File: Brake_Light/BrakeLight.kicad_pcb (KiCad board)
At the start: 2 copper layers, 99 x 20 mm, 38 parts, among them J2 Conn_01x01_Socket, J3 Conn_01x01_Socket, U1 LM317MABDTG

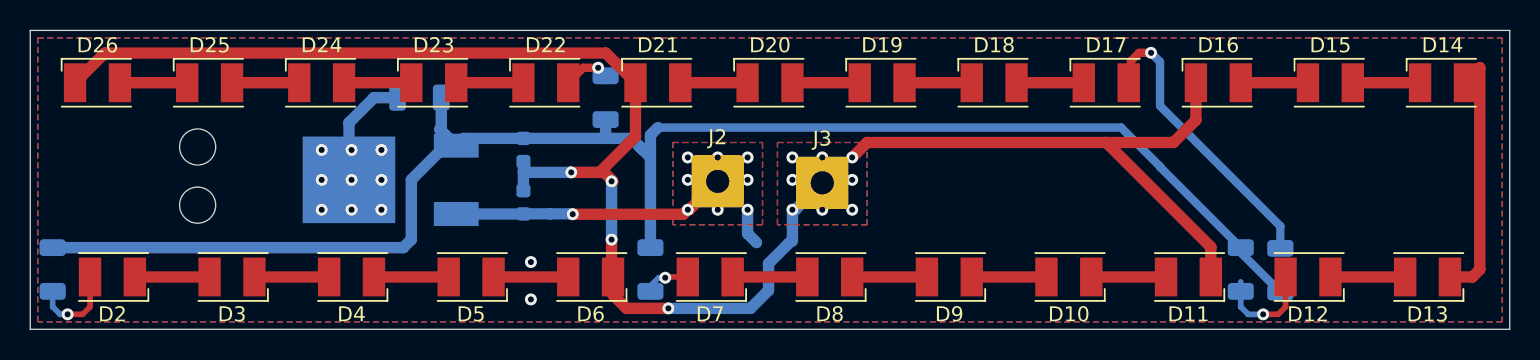
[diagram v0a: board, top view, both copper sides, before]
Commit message: Upgrade zones and via
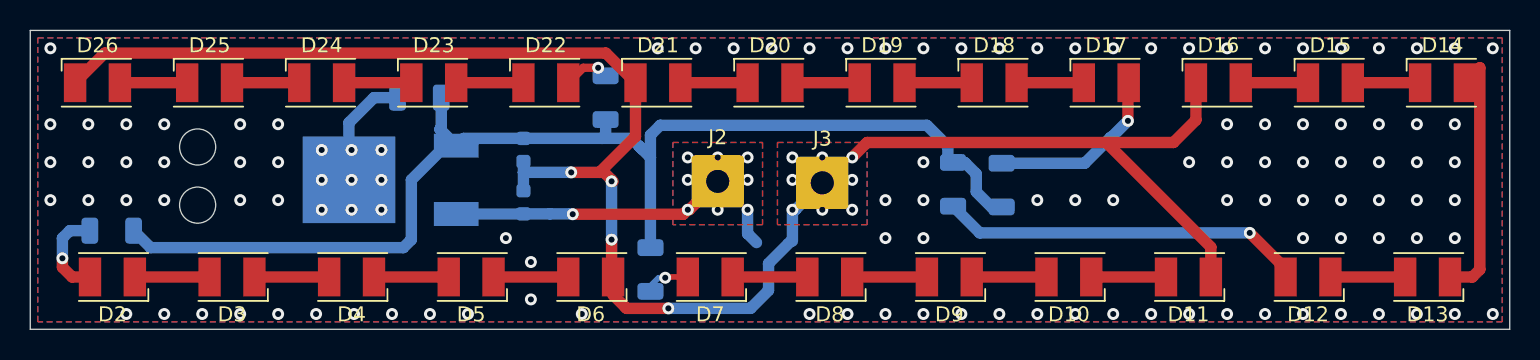
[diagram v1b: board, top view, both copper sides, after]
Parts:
- moved R4 20.1 mm to (117.8, 150.3)
- moved R5 19.5 mm to (121.0, 150.3)
- moved R1 4.73 mm to (61.5, 153.4), turned to 180 degrees
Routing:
- net /ADJ: track 106.0 -> 81.1 mm
- net Net-(D12-A): track 7.09 -> 24.5 mm
- net Net-(D17-A): track 19.8 -> 12.3 mm
- net Net-(D2-A): track 5.95 -> 6.71 mm
- net chłodzenie(Vout): vias 11 -> 119
